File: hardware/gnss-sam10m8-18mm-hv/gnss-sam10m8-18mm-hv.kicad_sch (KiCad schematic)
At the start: 33 parts, among them J3 BM05B-SRSS-TB, U1 SAM-M10Q-00B, U3 TPS62913RPUR

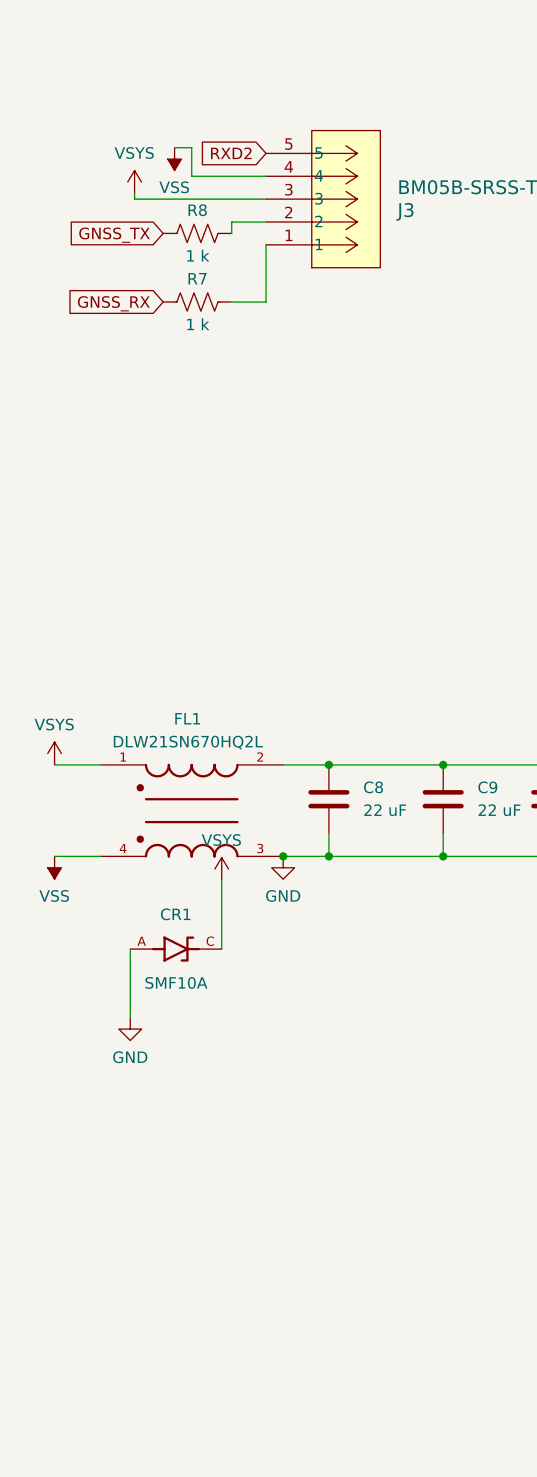
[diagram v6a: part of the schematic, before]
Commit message: hardware: sourcing + BOM-linkage metadata on the SMF10A symbol and all three instances
Library fields do not propagate to already-placed instances, so this writes
both: Custom.kicad_sym for future placements, and CR5 (LoRa) plus CR1 on each
GNSS board for the ones already drawn.

Fields follow the house convention rather than inventing names:

  MPN / Mfr   SMF10A / PTTC   the canonical pair -- what the cross-board BOM
                              audit joins on, and what 406 parts already carry
  Dist        LCSC            mirrors the sheet's own "Dist." column so the two
                              stay diff-checkable, same rationale as the
                              capacitor MinVRating pass
  Dist_PN     C5444308        the orderable key.  Named Dist_PN rather than the
                              LCSC_Part_Number four older symbols use, because
                              sourcing is mixed LCSC/DigiKey/Mouser and the
                              generic name survives a distributor change.
  Description full spec: 10 V standoff, 11.1 V VBR min, 17 V clamp at 11.8 A
                              Ipp, 200 W, SOD-123FL
  Notes       why 10 V and not 12 V -- SMF12A clamps 19.9 V, ABOVE the
                              TPS62913's 18 V VIN abs max, so it is not a
                              substitute despite looking like the same family

Two deliberate omissions. The SnapEDA-inherited MF / MP / MANUFACTURER /
STANDARD / PARTREV / SnapEDA_Link fields are NOT propagated -- that is exactly
where the two stale part numbers cleared in 59d2c67 were hiding, and a second
part-number field is the wrong-part-order hazard this fleet has already been
bitten by. Price is also left out: the BOM is the price authority, and a figure
copied into a symbol goes stale silently with nothing to catch it.

ERC clean on all three boards.

Co-Authored-By: Claude Opus 5 <noreply@anthropic.com>
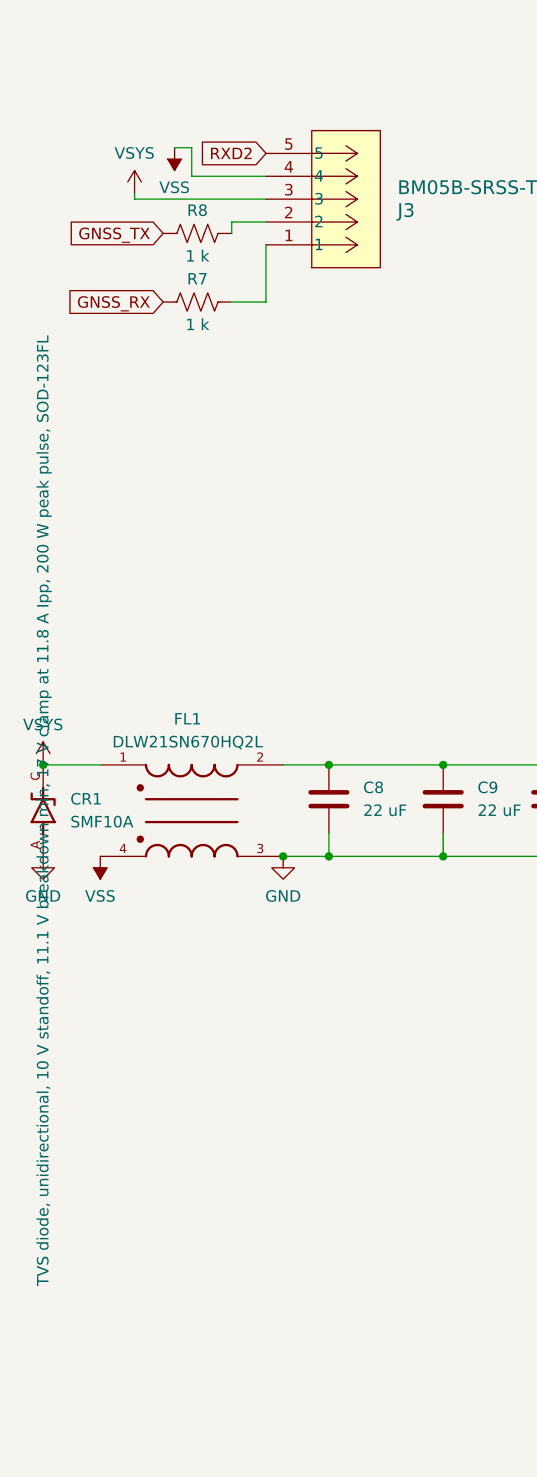
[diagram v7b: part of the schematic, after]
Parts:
- CR1: Dist (none) -> LCSC; Dist_PN (none) -> C5444308; Notes (none) -> Clamp must stay below the TPS62913 VIN abs max of 18 V. SMF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
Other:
- moved on the sheet: CR1

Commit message: hardware(gnss-sam10m8): pre-fab fixes -- TVS path, PSNS via, module stitching, PPS
Acts on the 2026-08-04 pre-manufacturing review. DRC after: 10 warnings
(5 lib_footprint_mismatch, 5 silk_over_copper), 0 unconnected items,
0 schematic-parity issues. Baseline was 9/0/0; the extra footprint mismatch is
R9 inheriting R2's library drift and is resolved separately.

A3 -- PSNS and PGND now have ground vias. TI SLVSFP4B 10.1 requires PSNS tied
to the plane with a via, and PSNS has the tightest absolute maximum on the part
(-0.3/+0.3 V). A via centred on the pad is not manufacturable here: U3's pads
are on a 0.5 mm pitch, leaving 0.248 mm between pad edges, so a via with 0.2 mm
clearance would need to be 0.34 mm -- below JLC's minimum. Both vias sit just
off the pad instead (0.15 mm for PSNS, 0.10 mm for PGND) on a short stub.

A4 -- V_BCKP left open per u-blox 4.1.3, with a no-connect flag. Also
no-connects on SAFEBOOT_N, SDA, SCL, EXTINT and PG, so ERC can tell deliberate
from forgotten. This removed 7 of the 11 ERC errors; the remaining 4 are
pre-existing power_pin_not_driven.

B1 -- CR1 moved from (46.105, 48.740) to (52.510, 54.665), under the connector,
and its anode moved from GND to VSS. The clamp path was
J3.3 -> CR1 -> GND -> FL1 winding 3-4 -> VSS -> J3.4, which put the choke's
common-mode impedance in the middle of the clamp and risked the part (320 mA
rating vs the SMF10A's 11.8 A). VSYS and VSS now run straight down from J3.3
and J3.4 as a 1 mm-spaced pair, so the transient loop is local and tightly
coupled. Note this is 5.24 mm from the connector rather than adjacent -- J3's
own courtyard is the binding constraint and no closer position exists in any
orientation.

B2 -- 11 GND vias added under the module (u-blox 4.4 asks for the plane below
it to be filled with vias); there were 5. Four more were generated but landed
inside the VO and +3V3 zone fills and were dropped.

B4 -- H1-H4 mounting pads assigned to GND. They were 3.8 mm of netless floating
copper on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
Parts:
- removed R4: 10 k, Resistor_SMD:R_0402_1005Metric, symbol Device:R_US
- added C16: 100 nF, Capacitor_SMD:C_0402_1005Metric, symbol Device:C
- added R9: 1 k, Resistor_SMD:R_0402_1005Metric, symbol Device:R_US
- H1, H2, H3, H4: symbol Mechanical:MountingHole -> Mechanical:MountingHole_Pad
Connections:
- net +3V3: now also C16.1; no longer U1.3 (V_BCKP)
- net GND: now also H1.1, H2.1, H3.1, H4.1, J3.6 (GND), J3.7 (GND), C16.2; no longer CR1.A
- net VSS: now also CR1.A
- net PPS: now reaches R1.1, U1.7 (TIMEPULSE)
- net PPS: now also R9.1
- net RXD2: no longer names the net of J3.5
- net RXD2: now also R9.2
- no-connect marks 0 -> 6
